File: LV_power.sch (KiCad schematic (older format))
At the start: 36 parts, among them T1 7508110151, U4 TPS76201, U5 TPS76201, U6 XCL221B18, U7 VIPER26HD

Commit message: Add more ceralinks on rear
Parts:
- renumbered C120 to C35, C35 to C36, C36 to C37, C37 to C38, C38 to C39, R81 to R20, R20 to R21, R21 to R22, R80 to R23, R22 to R24, R23 to R25
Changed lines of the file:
@@
 $EndDescr
 $Comp
-L +5VA #PWR62
+L +5VA #PWR60
 U 1 1 57A630DE
 P 8250 4700
-F 0 "#PWR62" H 8250 4550 50  0001 C CNN
+F 0 "#PWR60" H 8250 4550 50  0001 C CNN
 F 1 "+5VA" H 8265 4873 50  0000 C CNN
 F 2 "" H 8250 4700 50  0000 C CNN
@@
 $EndComp
 $Comp
-L R_Small R20
+L R_Small R21
 U 1 1 57A633D8
 P 8000 4850
-F 0 "R20" V 8196 4850 50  0000 C CNN
+F 0 "R21" V 8196 4850 50  0000 C CNN
 F 1 "FERRITE" V 8105 4850 50  0000 C CNN
 F 2 "Resistors_SMD:R_0805" H 8000 4850 50  0001 C CNN
@@
 $EndComp
 $Comp
-L GNDD #PWR63
+L GNDD #PWR57
 U 1 1 57A63878
 P 8550 1600
-F 0 "#PWR63" H 8550 1350 50  0001 C CNN
+F 0 "#PWR57" H 8550 1350 50  0001 C CNN
 F 1 "GNDD" H 8555 1427 50  0000 C CNN
 F 2 "" H 8550 1600 50  0000 C CNN
@@
 $EndComp
 $Comp
-L +3.3V #PWR64
+L +3.3V #PWR49
 U 1 1 57A63913
 P 9350 800
-F 0 "#PWR64" H 9350 650 50  0001 C CNN
+F 0 "#PWR49" H 9350 650 50  0001 C CNN
 F 1 "+3.3V" H 9365 973 50  0000 C CNN
 F 2 "" H 9350 800 50  0000 C CNN
@@
 $EndComp
 $Comp
-L +3.3VA #PWR58
+L +3.3VA #PWR47
 U 1 1 57F8E4FA
 P 6500 800
-F 0 "#PWR58" H 6500 650 50  0001 C CNN
+F 0 "#PWR47" H 6500 650 50  0001 C CNN
 F 1 "+3.3VA" H 6500 940 50  0000 C CNN
 F 2 "" H 6500 800 50  0000 C CNN
@@
 $EndComp
 $Comp
-L GNDD #PWR50
+L GNDD #PWR52
 U 1 1 57FAEA88
 P 3800 1050
-F 0 "#PWR50" H 3800 800 50  0001 C CNN
+F 0 "#PWR52" H 3800 800 50  0001 C CNN
 F 1 "GNDD" H 3805 877 50  0000 C CNN
 F 2 "" H 3800 1050 50  0000 C CNN
@@
 $EndComp
 $Comp
-L GNDD #PWR48
+L GNDD #PWR51
 U 1 1 57FAEAB4
 P 2600 1050
-F 0 "#PWR48" H 2600 800 50  0001 C CNN
+F 0 "#PWR51" H 2600 800 50  0001 C CNN
 F 1 "GNDD" H 2605 877 50  0000 C CNN
 F 2 "" H 2600 1050 50  0000 C CNN
@@
 $EndComp
 $Comp
-L +1V8 #PWR51
+L +1V8 #PWR54
 U 1 1 57FAFE13
 P 4150 1150
-F 0 "#PWR51" H 4150 1000 50  0001 C CNN
+F 0 "#PWR54" H 4150 1000 50  0001 C CNN
 F 1 "+1V8" H 4150 1290 50  0000 C CNN
 F 2 "" H 4150 1150 50  0000 C CNN
@@
 $EndComp
 $Comp
-L GNDD #PWR52
+L GNDD #PWR55
 U 1 1 57FAFE97
 P 4150 1350
-F 0 "#PWR52" H 4150 1100 50  0001 C CNN
+F 0 "#PWR55" H 4150 1100 50  0001 C CNN
 F 1 "GNDD" H 4155 1177 50  0000 C CNN
 F 2 "" H 4150 1350 50  0000 C CNN
@@
 $EndComp
 $Comp
-L GNDD #PWR47
+L GNDD #PWR53
 U 1 1 57FAFF6A
 P 1900 1150
-F 0 "#PWR47" H 1900 900 50  0001 C CNN
+F 0 "#PWR53" H 1900 900 50  0001 C CNN
 F 1 "GNDD" H 1905 977 50  0000 C CNN
 F 2 "" H 1900 1150 50  0000 C CNN
@@
 $EndComp
 $Comp
-L +5VD #PWR46
+L +5VD #PWR50
 U 1 1 57FB04EE
 P 1900 900
-F 0 "#PWR46" H 1900 750 50  0001 C CNN
+F 0 "#PWR50" H 1900 750 50  0001 C CNN
 F 1 "+5VD" H 1915 1073 50  0000 C CNN
 F 2 "" H 1900 900 50  0000 C CNN
@@
 $EndComp
 $Comp
-L +5VD #PWR60
+L +5VD #PWR48
 U 1 1 57FB15F5
 P 7900 800
-F 0 "#PWR60" H 7900 650 50  0001 C CNN
+F 0 "#PWR48" H 7900 650 50  0001 C CNN
 F 1 "+5VD" H 7915 973 50  0000 C CNN
 F 2 "" H 7900 800 50  0000 C CNN
@@
 $EndComp
 $Comp
-L GNDD #PWR57
+L GNDD #PWR56
 U 1 1 57FB234D
 P 5700 1600
-F 0 "#PWR57" H 5700 1350 50  0001 C CNN
+F 0 "#PWR56" H 5700 1350 50  0001 C CNN
 F 1 "GNDD" H 5705 1427 50  0000 C CNN
 F 2 "" H 5700 1600 50  0000 C CNN
@@
 $EndComp
 $Comp
-L +5VD #PWR56
+L +5VD #PWR46
 U 1 1 57FB236B
 P 5050 800
-F 0 "#PWR56" H 5050 650 50  0001 C CNN
+F 0 "#PWR46" H 5050 650 50  0001 C CNN
 F 1 "+5VD" H 5065 973 50  0000 C CNN
 F 2 "" H 5050 800 50  0000 C CNN
@@
 $EndComp
 $Comp
-L +5VD #PWR59
+L +5VD #PWR61
 U 1 1 57FB262C
 P 6950 4850
-F 0 "#PWR59" H 6950 4700 50  0001 C CNN
+F 0 "#PWR61" H 6950 4700 50  0001 C CNN
 F 1 "+5VD" H 6965 5023 50  0000 C CNN
 F 2 "" H 6950 4850 50  0000 C CNN
@@
 $EndComp
 $Comp
-L GNDD #PWR54
+L GNDD #PWR64
 U 1 1 57FB554E
 P 4250 5950
-F 0 "#PWR54" H 4250 5700 50  0001 C CNN
+F 0 "#PWR64" H 4250 5700 50  0001 C CNN
 F 1 "GNDD" H 4255 5777 50  0000 C CNN
 F 2 "" H 4250 5950 50  0000 C CNN
@@
 $EndComp
 $Comp
-L GNDD #PWR55
+L GNDD #PWR58
 U 1 1 57FB7D48
 P 4350 4050
-F 0 "#PWR55" H 4350 3800 50  0001 C CNN
+F 0 "#PWR58" H 4350 3800 50  0001 C CNN
 F 1 "GNDD" H 4355 3877 50  0000 C CNN
 F 2 "" H 4350 4050 50  0000 C CNN
@@
 $EndComp
 $Comp
-L R_Small R21
+L R_Small R22
 U 1 1 57FB9383
 P 4150 5100
-F 0 "R21" H 4180 5120 50  0000 L CNN
+F 0 "R22" H 4180 5120 50  0000 L CNN
 F 1 "17k" H 4180 5060 50  0000 L CNN
 F 2 "Resistors_SMD:R_0402" H 4150 5100 50  0001 C CNN
@@
 $EndComp
 $Comp
-L R_Small R23
+L R_Small R25
 U 1 1 57FB9389
 P 4150 5300
-F 0 "R23" H 4180 5320 50  0000 L CNN
+F 0 "R25" H 4180 5320 50  0000 L CNN
 F 1 "33k" H 4180 5260 50  0000 L CNN
 F 2 "Resistors_SMD:R_0402" H 4150 5300 50  0001 C CNN
@@
 $EndComp
 $Comp
-L C C35
+L C C36
 U 1 1 57FB9EE1
 P 6950 5050
-F 0 "C35" H 6975 5150 50  0000 L CNN
+F 0 "C36" H 6975 5150 50  0000 L CNN
 F 1 "100uF 16V" H 6975 4950 50  0000 L CNN
 F 2 "sictroller:C_6x5" H 6988 4900 50  0001 C CNN
@@
 $EndComp
 $Comp
-L +5VD #PWR53
+L +5VD #PWR62
 U 1 1 57FBA909
 P 4150 5000
-F 0 "#PWR53" H 4150 4850 50  0001 C CNN
+F 0 "#PWR62" H 4150 4850 50  0001 C CNN
 F 1 "+5VD" H 4165 5173 50  0000 C CNN
 F 2 "" H 4150 5000 50  0000 C CNN
@@
 $EndComp
 $Comp
-L C C38
+L C C39
 U 1 1 57FBBD5D
 P 4450 5650
-F 0 "C38" H 4475 5750 50  0000 L CNN
+F 0 "C39" H 4475 5750 50  0000 L CNN
 F 1 "1uF 30V" H 4475 5550 50  0000 L CNN
 F 2 "Capacitors_SMD:C_0603" H 4488 5500 50  0001 C CNN
@@
 $EndComp
 $Comp
-L R_Small R22
+L R_Small R24
 U 1 1 57FBD333
 P 2800 5250
-F 0 "R22" H 2830 5270 50  0000 L CNN
+F 0 "R24" H 2830 5270 50  0000 L CNN
 F 1 "3.3k" H 2830 5210 50  0000 L CNN
 F 2 "Resistors_SMD:R_0402" H 2800 5250 50  0001 C CNN
@@
 $EndComp
 $Comp
-L C C36
+L C C37
 U 1 1 57FBD40D
 P 2800 5500
-F 0 "C36" H 2825 5600 50  0000 L CNN
+F 0 "C37" H 2825 5600 50  0000 L CNN
 F 1 "47nF" H 2825 5400 50  0000 L CNN
 F 2 "Capacitors_SMD:C_0402" H 2838 5350 50  0001 C CNN
@@
 $EndComp
 $Comp
-L C C37
+L C C38
 U 1 1 57FBD4FF
 P 3150 5500
-F 0 "C37" H 3175 5600 50  0000 L CNN
+F 0 "C38" H 3175 5600 50  0000 L CNN
 F 1 "2.2nF" H 3175 5400 50  0000 L CNN
 F 2 "Capacitors_SMD:C_0402" H 3188 5350 50  0001 C CNN
@@
 $EndComp
 $Comp
-L GNDD #PWR49
+L GNDD #PWR59
 U 1 1 57FCE56A
 P 2600 4350
-F 0 "#PWR49" H 2600 4100 50  0001 C CNN
+F 0 "#PWR59" H 2600 4100 50  0001 C CNN
 F 1 "GNDD" H 2600 4200 50  0000 C CNN
 F 2 "" H 2600 4350 50  0000 C CNN
@@
 COMP
 $Comp
-L R_Small R80
+L R_Small R23
 U 1 1 5804A7B3
 P 2300 5250
-F 0 "R80" H 2330 5270 50  0000 L CNN
+F 0 "R23" H 2330 5270 50  0000 L CNN
 F 1 "DNP" H 2330 5210 50  0000 L CNN
 F 2 "Resistors_SMD:R_0402" H 2300 5250 50  0001 C CNN
@@
 	2300 4550 3250 4550
 $Comp
-L R_Small R81
+L R_Small R20
 U 1 1 57F9585B
 P 4850 4050
-F 0 "R81" H 4880 4070 50  0000 L CNN
+F 0 "R20" H 4880 4070 50  0000 L CNN
 F 1 "51k" H 4880 4010 50  0000 L CNN
 F 2 "Resistors_SMD:R_1206" H 4850 4050 50  0001 C CNN
@@
 Connection ~ 4850 3950
 $Comp
-L C C120
+L C C35
 U 1 1 57F987E3
 P 8200 5000
-F 0 "C120" H 8225 5100 50  0000 L CNN
+F 0 "C35" H 8225 5100 50  0000 L CNN
 F 1 "10uF 16V" H 8225 4900 50  0000 L CNN
 F 2 "Capacitors_SMD:C_0805" H 8238 4850 50  0001 C CNN
@@
 $EndComp
 $Comp
-L GNDD #PWR61
+L GNDD #PWR63
 U 1 1 57F99976
 P 8200 5150
-F 0 "#PWR61" H 8200 4900 50  0001 C CNN
+F 0 "#PWR63" H 8200 4900 50  0001 C CNN
 F 1 "GNDD" H 8205 4977 50  0000 C CNN
 F 2 "" H 8200 5150 50  0000 C CNN

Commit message: some logic placement progress
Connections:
- net +5VA: now also C28.1, U4.1 (VIN)
- net +5VD: now also U6.8 (L2); no longer C28.1, U4.1 (VIN), U6.7 (L1)
- net GNDD: no longer C28.2, C29.2, C35.2, R16.2, U4.2 (GND), U4.3 (EN)
- net at U6.1 (Lx): now also U6.7 (L1); no longer U6.8 (L2)
- new net GNDA: C28.2, C29.2, C35.2, R16.2, U4.2 (GND), U4.3 (EN)
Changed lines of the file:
@@
 $EndDescr
 $Comp
-L +5VA #PWR049
+L +5VA #PWR053
 U 1 1 57A630DE
 P 8250 4700
-F 0 "#PWR049" H 8250 4550 50  0001 C CNN
+F 0 "#PWR053" H 8250 4550 50  0001 C CNN
 F 1 "+5VA" H 8265 4873 50  0000 C CNN
 F 2 "" H 8250 4700 50  0000 C CNN
@@
 $EndComp
 $Comp
-L GNDD #PWR050
+L GNDD #PWR054
 U 1 1 57A63878
 P 8550 1600
-F 0 "#PWR050" H 8550 1350 50  0001 C CNN
+F 0 "#PWR054" H 8550 1350 50  0001 C CNN
 F 1 "GNDD" H 8555 1427 50  0000 C CNN
 F 2 "" H 8550 1600 50  0000 C CNN
@@
 $EndComp
 $Comp
-L +3.3V #PWR051
+L +3.3V #PWR055
 U 1 1 57A63913
 P 9350 800
-F 0 "#PWR051" H 9350 650 50  0001 C CNN
+F 0 "#PWR055" H 9350 650 50  0001 C CNN
 F 1 "+3.3V" H 9365 973 50  0000 C CNN
 F 2 "" H 9350 800 50  0000 C CNN
@@
 $EndComp
 $Comp
-L PWR_FLAG #FLG052
+L PWR_FLAG #FLG056
 U 1 1 57A8371C
 P 8250 4850
-F 0 "#FLG052" H 8250 4945 50  0001 C CNN
+F 0 "#FLG056" H 8250 4945 50  0001 C CNN
 F 1 "PWR_FLAG" V 8250 5028 50  0000 L CNN
 F 2 "" H 8250 4850 50  0000 C CNN
@@
 $EndComp
 $Comp
-L +3.3VA #PWR053
+L +3.3VA #PWR057
 U 1 1 57F8E4FA
 P 6500 800
-F 0 "#PWR053" H 6500 650 50  0001 C CNN
+F 0 "#PWR057" H 6500 650 50  0001 C CNN
 F 1 "+3.3VA" H 6500 940 50  0000 C CNN
 F 2 "" H 6500 800 50  0000 C CNN
@@
 $EndComp
 $Comp
-L GNDD #PWR054
+L GNDD #PWR058
 U 1 1 57FAEA88
 P 3800 1050
-F 0 "#PWR054" H 3800 800 50  0001 C CNN
+F 0 "#PWR058" H 3800 800 50  0001 C CNN
 F 1 "GNDD" H 3805 877 50  0000 C CNN
 F 2 "" H 3800 1050 50  0000 C CNN
@@
 $EndComp
 $Comp
-L GNDD #PWR055
+L GNDD #PWR059
 U 1 1 57FAEAB4
 P 2600 1050
-F 0 "#PWR055" H 2600 800 50  0001 C CNN
+F 0 "#PWR059" H 2600 800 50  0001 C CNN
 F 1 "GNDD" H 2605 877 50  0000 C CNN
 F 2 "" H 2600 1050 50  0000 C CNN
@@
 $EndComp
 $Comp
-L +1V8 #PWR056
+L +1V8 #PWR060
 U 1 1 57FAFE13
 P 4150 1150
-F 0 "#PWR056" H 4150 1000 50  0001 C CNN
+F 0 "#PWR060" H 4150 1000 50  0001 C CNN
 F 1 "+1V8" H 4150 1290 50  0000 C CNN
 F 2 "" H 4150 1150 50  0000 C CNN
@@
 $EndComp
 $Comp
-L GNDD #PWR057
+L GNDD #PWR061
 U 1 1 57FAFE97
 P 4150 1350
-F 0 "#PWR057" H 4150 1100 50  0001 C CNN
+F 0 "#PWR061" H 4150 1100 50  0001 C CNN
 F 1 "GNDD" H 4155 1177 50  0000 C CNN
 F 2 "" H 4150 1350 50  0000 C CNN
@@
 $EndComp
 $Comp
-L GNDD #PWR058
+L GNDD #PWR062
 U 1 1 57FAFF6A
 P 1900 1150
-F 0 "#PWR058" H 1900 900 50  0001 C CNN
+F 0 "#PWR062" H 1900 900 50  0001 C CNN
 F 1 "GNDD" H 1905 977 50  0000 C CNN
 F 2 "" H 1900 1150 50  0000 C CNN
@@
 $EndComp
 $Comp
-L +5VD #PWR059
+L +5VD #PWR063
 U 1 1 57FB04EE
 P 1900 900
-F 0 "#PWR059" H 1900 750 50  0001 C CNN
+F 0 "#PWR063" H 1900 750 50  0001 C CNN
 F 1 "+5VD" H 1915 1073 50  0000 C CNN
 F 2 "" H 1900 900 50  0000 C CNN
@@
 $EndComp
 $Comp
-L +5VD #PWR060
+L +5VD #PWR064
 U 1 1 57FB15F5
 P 7900 800
-F 0 "#PWR060" H 7900 650 50  0001 C CNN
+F 0 "#PWR064" H 7900 650 50  0001 C CNN
 F 1 "+5VD" H 7915 973 50  0000 C CNN
 F 2 "" H 7900 800 50  0000 C CNN
@@
 $EndComp
 $Comp
-L GNDD #PWR061
-U 1 1 57FB234D
-P 5700 1600
-F 0 "#PWR061" H 5700 1350 50  0001 C CNN
-F 1 "GNDD" H 5705 1427 50  0000 C CNN
-F 2 "" H 5700 1600 50  0000 C CNN
-F 3 "" H 5700 1600 50  0000 C CNN
-	1    5700 1600
-	1    0    0    -1
-$EndComp
-$Comp
 L C_Small C29
 U 1 1 57FB2359
@@
 $EndComp
 $Comp
-L +5VD #PWR062
-U 1 1 57FB236B
-P 5050 800
-F 0 "#PWR062" H 5050 650 50  0001 C CNN
-F 1 "+5VD" H 5065 973 50  0000 C CNN
-F 2 "" H 5050 800 50  0000 C CNN
-F 3 "" H 5050 800 50  0000 C CNN
-	1    5050 800
-	1    0    0    -1
-$EndComp
-$Comp
 L R_Small R14
 U 1 1 57FB2371
@@
 $EndComp
 $Comp
-L +5VD #PWR063
+L +5VD #PWR065
 U 1 1 57FB262C
 P 6950 4850
-F 0 "#PWR063" H 6950 4700 50  0001 C CNN
+F 0 "#PWR065" H 6950 4700 50  0001 C CNN
 F 1 "+5VD" H 6965 5023 50  0000 C CNN
 F 2 "" H 6950 4850 50  0000 C CNN
@@
 $EndComp
 $Comp
-L GNDD #PWR064
+L GNDD #PWR066
 U 1 1 57FB554E
 P 4250 5950
-F 0 "#PWR064" H 4250 5700 50  0001 C CNN
+F 0 "#PWR066" H 4250 5700 50  0001 C CNN
 F 1 "GNDD" H 4255 5777 50  0000 C CNN
 F 2 "" H 4250 5950 50  0000 C CNN
@@
 $EndComp
 $Comp
-L GNDD #PWR065
+L GNDD #PWR067
 U 1 1 57FB7D48
 P 4350 4050
-F 0 "#PWR065" H 4350 3800 50  0001 C CNN
+F 0 "#PWR067" H 4350 3800 50  0001 C CNN
 F 1 "GNDD" H 4355 3877 50  0000 C CNN
 F 2 "" H 4350 4050 50  0000 C CNN
@@
 $EndComp
 $Comp
-L +5VD #PWR066
+L +5VD #PWR068
 U 1 1 57FBA909
 P 4150 5000
-F 0 "#PWR066" H 4150 4850 50  0001 C CNN
+F 0 "#PWR068" H 4150 4850 50  0001 C CNN
 F 1 "+5VD" H 4165 5173 50  0000 C CNN
 F 2 "" H 4150 5000 50  0000 C CNN
@@
 $EndComp
 $Comp
-L PWR_FLAG #FLG067
+L PWR_FLAG #FLG069
 U 1 1 57FBE4C9
 P 7350 4850
-F 0 "#FLG067" H 7350 4945 50  0001 C CNN
+F 0 "#FLG069" H 7350 4945 50  0001 C CNN
 F 1 "PWR_FLAG" V 7350 5028 50  0000 L CNN
 F 2 "" H 7350 4850 50  0000 C CNN
@@
 $EndComp
 $Comp
-L GNDD #PWR068
+L GNDD #PWR070
 U 1 1 57FCE56A
 P 2600 4350
-F 0 "#PWR068" H 2600 4100 50  0001 C CNN
+F 0 "#PWR070" H 2600 4100 50  0001 C CNN
 F 1 "GNDD" H 2600 4200 50  0000 C CNN
 F 2 "" H 2600 4350 50  0000 C CNN
@@
 $EndComp
 $Comp
-L PWR_FLAG #FLG069
+L PWR_FLAG #FLG071
 U 1 1 57FCEFC8
 P 2700 4350
-F 0 "#FLG069" H 2700 4445 50  0001 C CNN
+F 0 "#FLG071" H 2700 4445 50  0001 C CNN
 F 1 "PWR_FLAG" V 2700 4528 50  0000 L CNN
 F 2 "" H 2700 4350 50  0000 C CNN
@@
 	2700 750  2700 950
 Wire Wire Line
-	2700 750  3200 750
-Wire Wire Line
 	2600 1050 2700 1050
 Wire Wire Line
@@
 Wire Wire Line
 	4150 1150 3700 1150
-Wire Wire Line
-	3200 1350 3750 1350
-Wire Wire Line
-	3750 1350 3750 950
 Wire Wire Line
 	3750 950  3700 950
@@
 	5050 800  5050 1300
 Wire Wire Line
-	5700 1600 5700 1550
-Wire Wire Line
 	6500 800  6500 1300
 Wire Wire Line
@@
 Wire Wire Line
 	5050 1550 5050 1500
-Connection ~ 5700 1550
 Wire Wire Line
 	5750 1300 5750 1550
@@
 	1    0    0    -1
 $EndComp
-$Comp
-L GNDD #PWR070
-U 1 1 57F99976
+Connection ~ 8200 4850
+$Comp
+L GNDA #PWR072
+U 1 1 58070218
 P 8200 5150
-F 0 "#PWR070" H 8200 4900 50  0001 C CNN
-F 1 "GNDD" H 8205 4977 50  0000 C CNN
+F 0 "#PWR072" H 8200 4900 50  0001 C CNN
+F 1 "GNDA" H 8200 5000 50  0000 C CNN
 F 2 "" H 8200 5150 50  0000 C CNN
 F 3 "" H 8200 5150 50  0000 C CNN
@@
 	1    0    0    -1
 $EndComp
-Connection ~ 8200 4850
+$Comp
+L GNDA #PWR073
+U 1 1 58070422
+P 5950 1600
+F 0 "#PWR073" H 5950 1350 50  0001 C CNN
+F 1 "GNDA" H 5950 1450 50  0000 C CNN
+F 2 "" H 5950 1600 50  0000 C CNN
+F 3 "" H 5950 1600 50  0000 C CNN
+	1    5950 1600
+	1    0    0    -1
+$EndComp
+Wire Wire Line
+	5950 1600 5950 1550
+Connection ~ 5950 1550
+$Comp
+L +5VA #PWR074
+U 1 1 58070B6B
+P 5050 800
+F 0 "#PWR074" H 5050 650 50  0001 C CNN
+F 1 "+5VA" H 5065 973 50  0000 C CNN
+F 2 "" H 5050 800 50  0000 C CNN
+F 3 "" H 5050 800 50  0000 C CNN
+	1    5050 800
+	1    0    0    -1
+$EndComp
+Wire Wire Line
+	3750 950  3750 750
+Wire Wire Line
+	3750 750  3200 750
+Wire Wire Line
+	3200 1350 3000 1350
+Wire Wire Line
+	3000 1350 3000 750
+Wire Wire Line
+	3000 750  2700 750
 $EndSCHEMATC

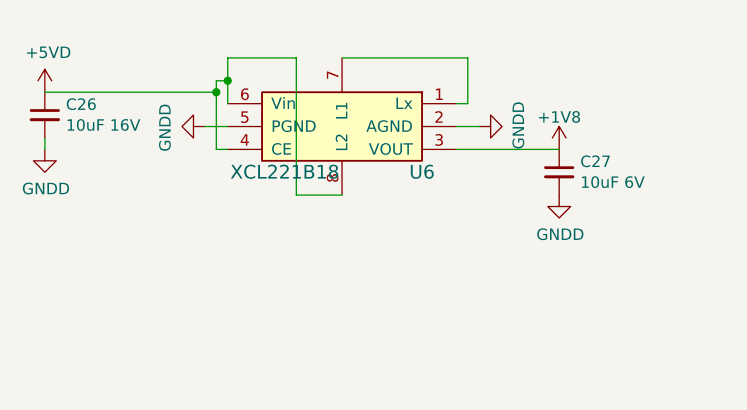
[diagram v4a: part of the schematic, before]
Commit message: 3.3V and 1.8V supplies routed; fixed wrong connections on 1.8V regulator
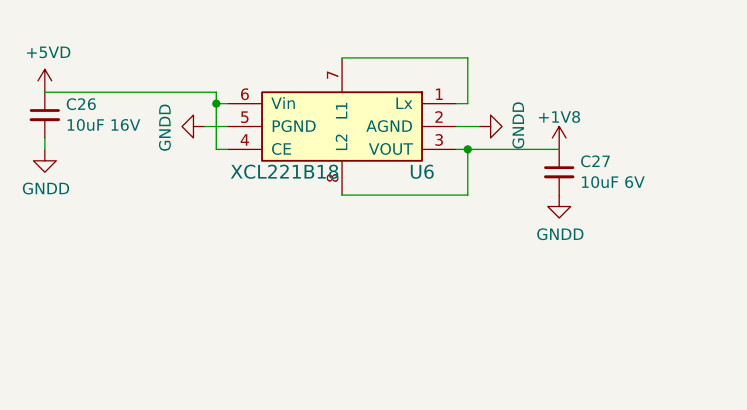
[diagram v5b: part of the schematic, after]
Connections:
- net +1V8: now also U6.8 (L2)
- net +5VD: no longer U6.8 (L2)
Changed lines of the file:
@@
 Connection ~ 8550 1550
 Wire Wire Line
-	2700 750  2700 950
-Wire Wire Line
 	2600 1050 2700 1050
 Wire Wire Line
 	2650 1150 2700 1150
 Wire Wire Line
-	2650 850  2650 1150
-Wire Wire Line
-	2650 850  2700 850
-Connection ~ 2700 850
-Wire Wire Line
 	4150 1150 3700 1150
 Wire Wire Line
@@
 Wire Wire Line
 	1900 900  2650 900
-Connection ~ 2650 900
 Wire Wire Line
 	8600 1300 8600 1550
@@
 	3750 750  3200 750
 Wire Wire Line
-	3200 1350 3000 1350
-Wire Wire Line
-	3000 1350 3000 750
-Wire Wire Line
-	3000 750  2700 750
+	2650 900  2650 1150
+Wire Wire Line
+	2650 950  2700 950
+Connection ~ 2650 950
+Wire Wire Line
+	3200 1350 3750 1350
+Wire Wire Line
+	3750 1350 3750 1150
+Connection ~ 3750 1150
 $EndSCHEMATC

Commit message: As sent to Tempo 2016-10-21
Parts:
- R14, R15: value 264k -> 42.2k
- R16: value 66.5k -> 10.7kk
- R17: value 66.5k -> 10.7k
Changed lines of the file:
@@
 F 0 "U5" H 8350 1200 50  0000 L CNN
 F 1 "TPS76201" H 8900 1200 50  0000 R CNN
-F 2 "TO_SOT_Packages_SMD:SOT-23-5" H 8850 750 50  0000 C CIN
+F 2 "TO_SOT_Packages_SMD:SOT-23-5" H 8850 750 50  0001 C CIN
 F 3 "" H 8600 1000 50  0000 C CNN
 	1    8600 1000
@@
 P 9100 1000
 F 0 "R15" H 9130 1020 50  0000 L CNN
-F 1 "264k" H 9130 960 50  0000 L CNN
+F 1 "42.2k" H 9130 960 50  0000 L CNN
 F 2 "Resistors_SMD:R_0402" H 9100 1000 50  0001 C CNN
 F 3 "" H 9100 1000 50  0000 C CNN
@@
 P 9100 1200
 F 0 "R17" H 9130 1220 50  0000 L CNN
-F 1 "66.5k" H 9130 1160 50  0000 L CNN
+F 1 "10.7k" H 9130 1160 50  0000 L CNN
 F 2 "Resistors_SMD:R_0402" H 9100 1200 50  0001 C CNN
 F 3 "" H 9100 1200 50  0000 C CNN
@@
 F 0 "U4" H 5500 1200 50  0000 L CNN
 F 1 "TPS76201" H 6050 1200 50  0000 R CNN
-F 2 "TO_SOT_Packages_SMD:SOT-23-5" H 6000 750 50  0000 C CIN
+F 2 "TO_SOT_Packages_SMD:SOT-23-5" H 6000 750 50  0001 C CIN
 F 3 "" H 5750 1000 50  0000 C CNN
 	1    5750 1000
@@
 P 6250 1000
 F 0 "R14" H 6280 1020 50  0000 L CNN
-F 1 "264k" H 6280 960 50  0000 L CNN
+F 1 "42.2k" H 6280 960 50  0000 L CNN
 F 2 "Resistors_SMD:R_0402" H 6250 1000 50  0001 C CNN
 F 3 "" H 6250 1000 50  0000 C CNN
@@
 P 6250 1200
 F 0 "R16" H 6280 1220 50  0000 L CNN
-F 1 "66.5k" H 6280 1160 50  0000 L CNN
+F 1 "10.7kk" H 6280 1160 50  0000 L CNN
 F 2 "Resistors_SMD:R_0402" H 6250 1200 50  0001 C CNN
 F 3 "" H 6250 1200 50  0000 C CNN
